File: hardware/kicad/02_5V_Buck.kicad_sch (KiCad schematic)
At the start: 11 parts, among them U101 LMR38020SQDDARQ1

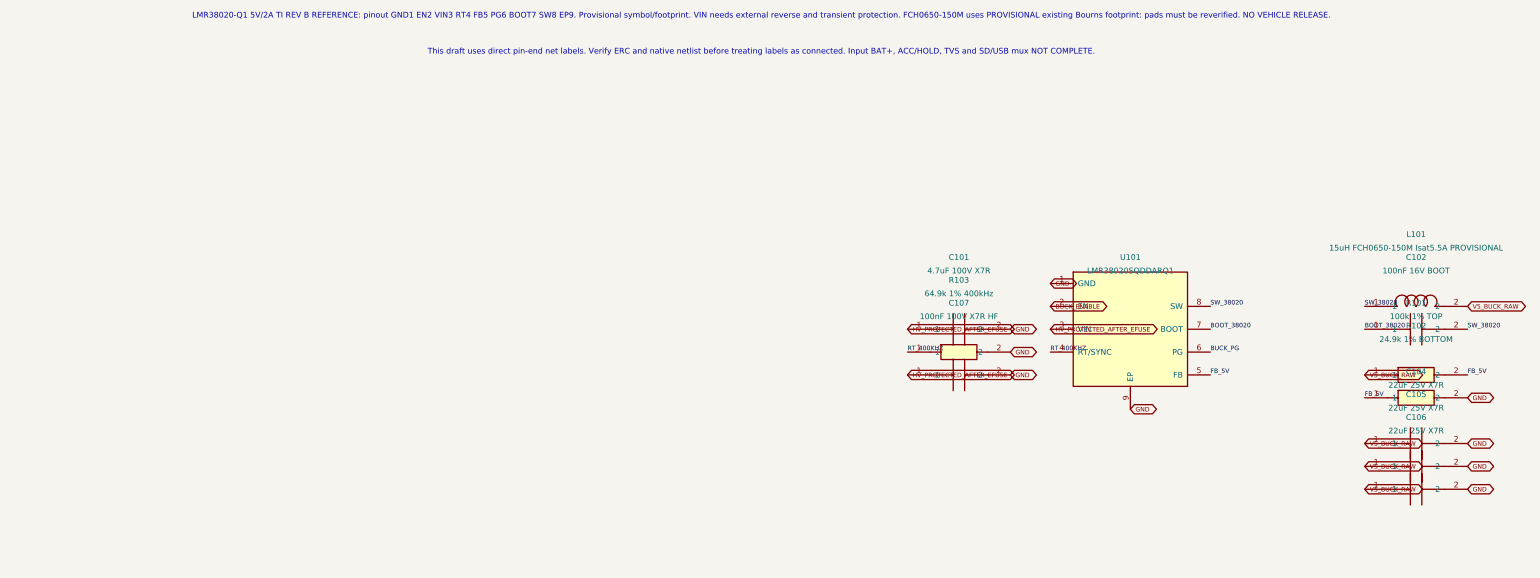
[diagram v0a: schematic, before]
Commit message: fix(power): explicitly leave optional LMR38020 PG open-drain floating per TI; remove isolated dummy signal
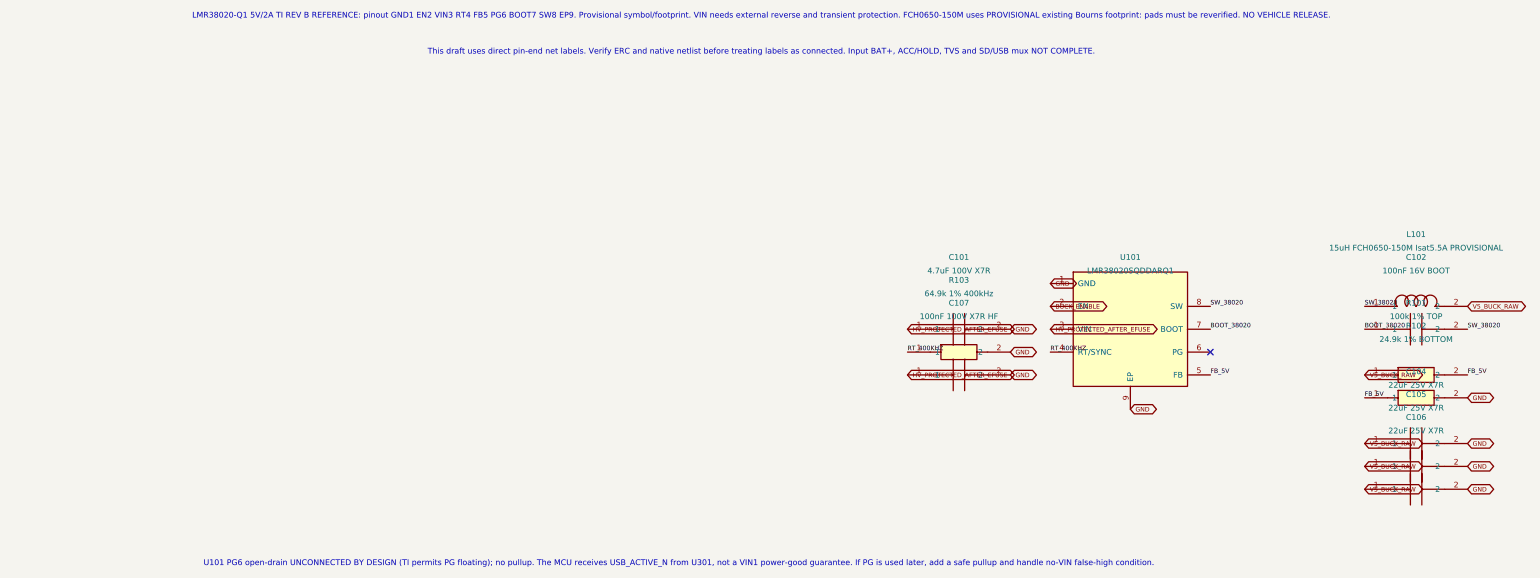
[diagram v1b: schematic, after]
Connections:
- net BUCK_PG: no longer names the net of U101.6 (PG)
- no-connect marks 0 -> 1
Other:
- note added: "U101 PG6 open-drain UNCONNECTED BY DESIGN (TI permits PG floating); no pullup. The MCU receives USB_ACTIVE_N from U301, not a VIN1 power-good guarantee. If PG is used later, add a safe pullup and handle no-VIN false-high condition."

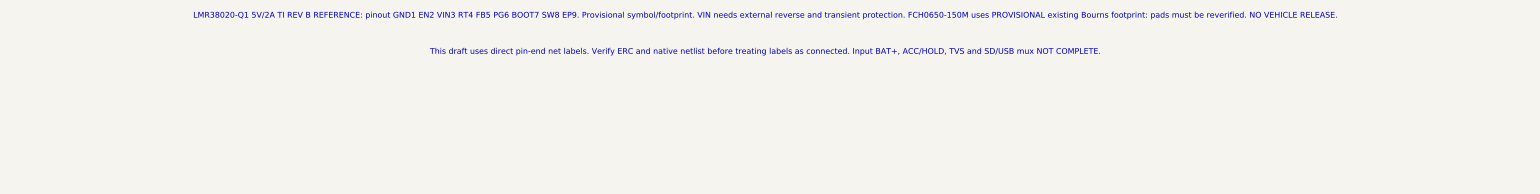
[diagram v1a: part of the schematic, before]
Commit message: engineering: decide COTS buck baseline, document protection release gates and verify installed MPNs
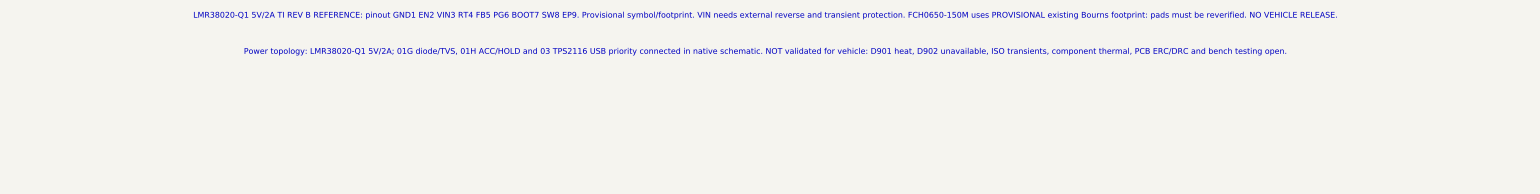
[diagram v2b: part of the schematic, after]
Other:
- note added: "Power topology: LMR38020-Q1 5V/2A; 01G diode/TVS, 01H ACC/HOLD and 03 TPS2116 USB priority connected in native schematic. NOT validated for vehicle: D901 heat, D902 unavailable, ISO transients, component thermal, PCB ERC/DRC and bench testing open."
- note removed: "This draft uses direct pin-end net labels. Verify ERC and native netlist before treating labels as connected. Input BAT+, ACC/HOLD, TVS and SD/USB mux NOT COMPLETE."

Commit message: fix(kicad): repair LMR38020-Q1 U101 physical PCB pin nets and audit via CI
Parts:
- U101: footprint Package_SO:SOIC-8-1EP_3.9x4.9mm_P1.27mm_EP2.29x3mm -> Tripmaster:TI_LMR38020Q1_DDA_EP

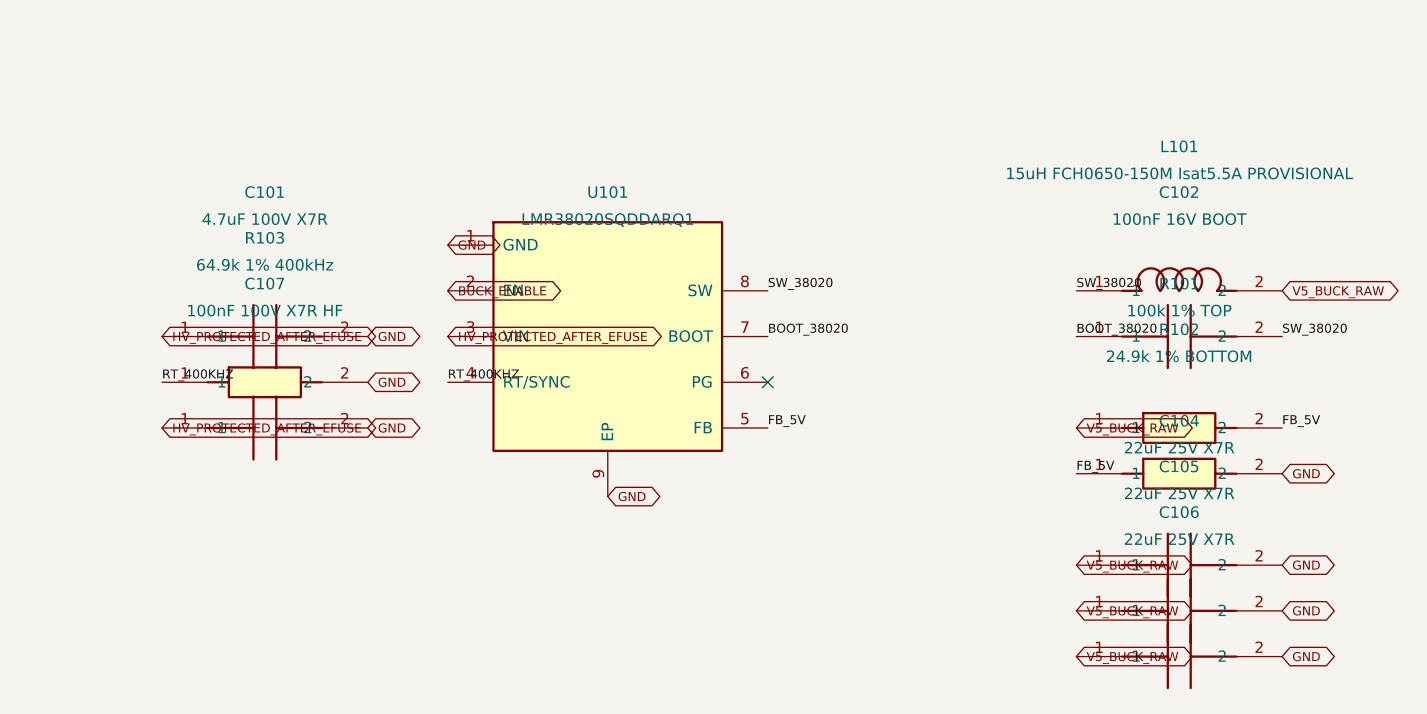
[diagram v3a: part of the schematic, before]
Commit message: hardware(buck): add C108 second VIN 4.7uF capacitor, synchronize 15uH and MPN fields
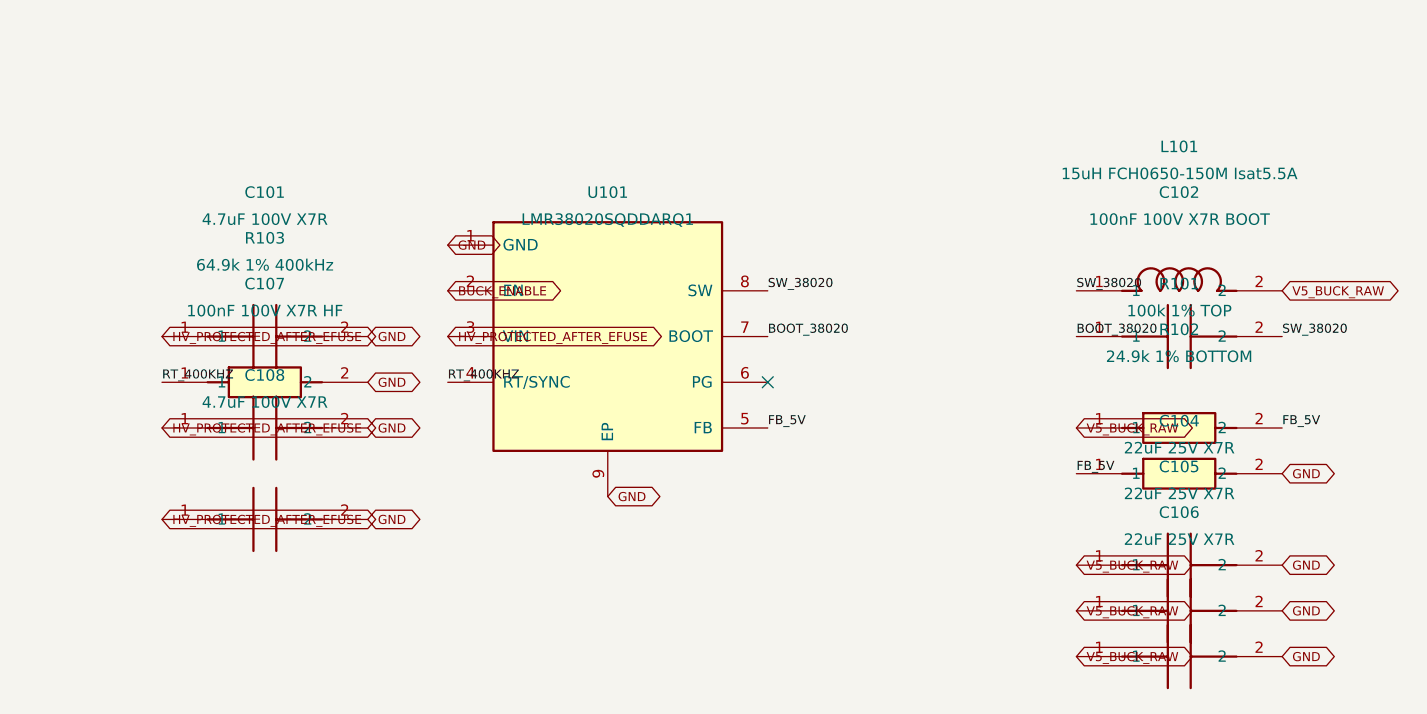
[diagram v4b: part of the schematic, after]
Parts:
- added C108: 4.7uF 100V X7R, Tripmaster:C_1210_3225, symbol Tripmaster_Sym:C1210
- C101: MPN (none) -> 12101C475K4Z2A
- C102: value 100nF 16V BOOT -> 100nF 100V X7R BOOT; MPN (none) -> C1206C104K1RACTU
- C104, C105, C106: MPN (none) -> GRM32ER71E226KE15L
- C107: MPN (none) -> C1206C104K1RACTU
- L101: value 15uH FCH0650-150M Isat5.5A PROVISIONAL -> 15uH FCH0650-150M Isat5.5A; footprint Tripmaster:L_Bourns_SRP6030VA_100M -> Tripmaster:L_FANGCHENG_FCH0650_150M; MPN (none) -> FCH0650-150M
- R101: MPN (none) -> RC1206FR-07100KL
- R102: MPN (none) -> RC1206FR-0724K9L
- R103: MPN (none) -> RC1206FR-0764K9L
- U101: MPN (none) -> LMR38020SQDDARQ1
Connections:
- net GND: now also C108.2
- net HV_PROTECTED_AFTER_EFUSE: now also C108.1

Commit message: hardware(buck): mark C108 manufacturer MPN same as C101
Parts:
- C108: MPN (none) -> 12101C475K4Z2A

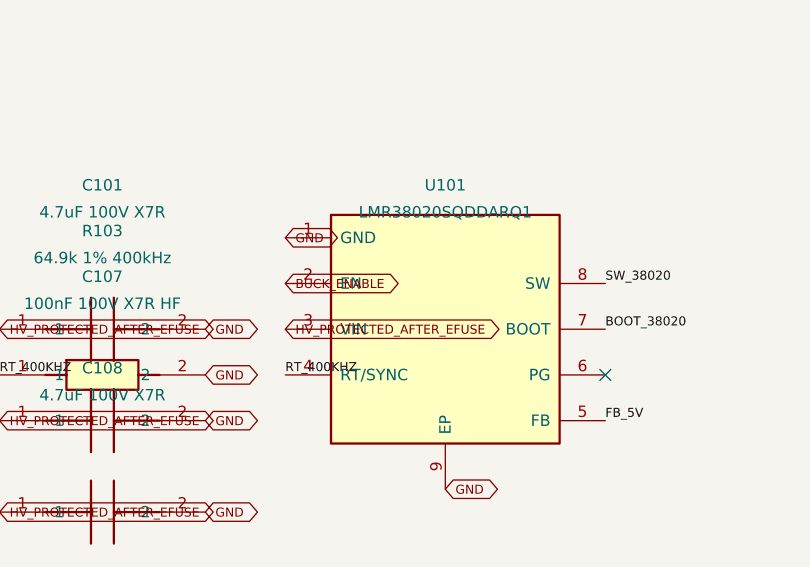
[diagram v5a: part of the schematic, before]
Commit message: fix(critical): tie LMR38020 EN to its own protected VIN, prevent VIN-off/EN-high absolute maximum violation
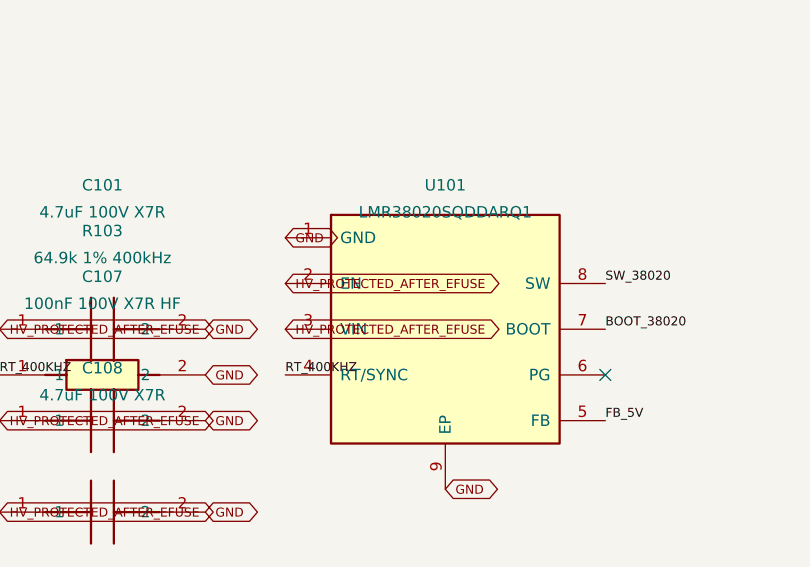
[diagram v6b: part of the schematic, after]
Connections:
- net BUCK_ENABLE is gone; now on net HV_PROTECTED_AFTER_EFUSE: U101.2 (EN)
